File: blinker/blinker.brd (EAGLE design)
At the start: 36.5 x 64.8 mm, 11 parts, among them IC1 LM555D, SW1 SPST_TACT5.2VARIANT

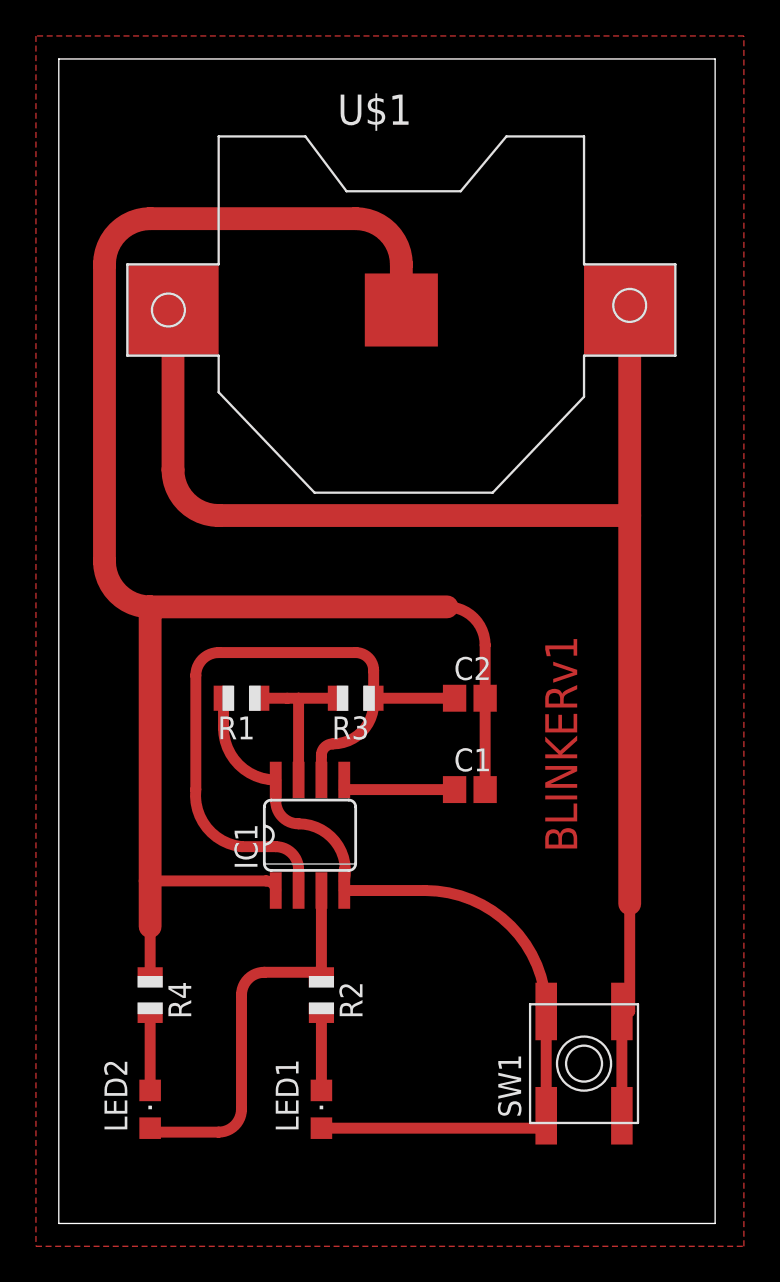
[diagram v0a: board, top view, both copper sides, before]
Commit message: CR2032 Batt holder amended, PCB design update
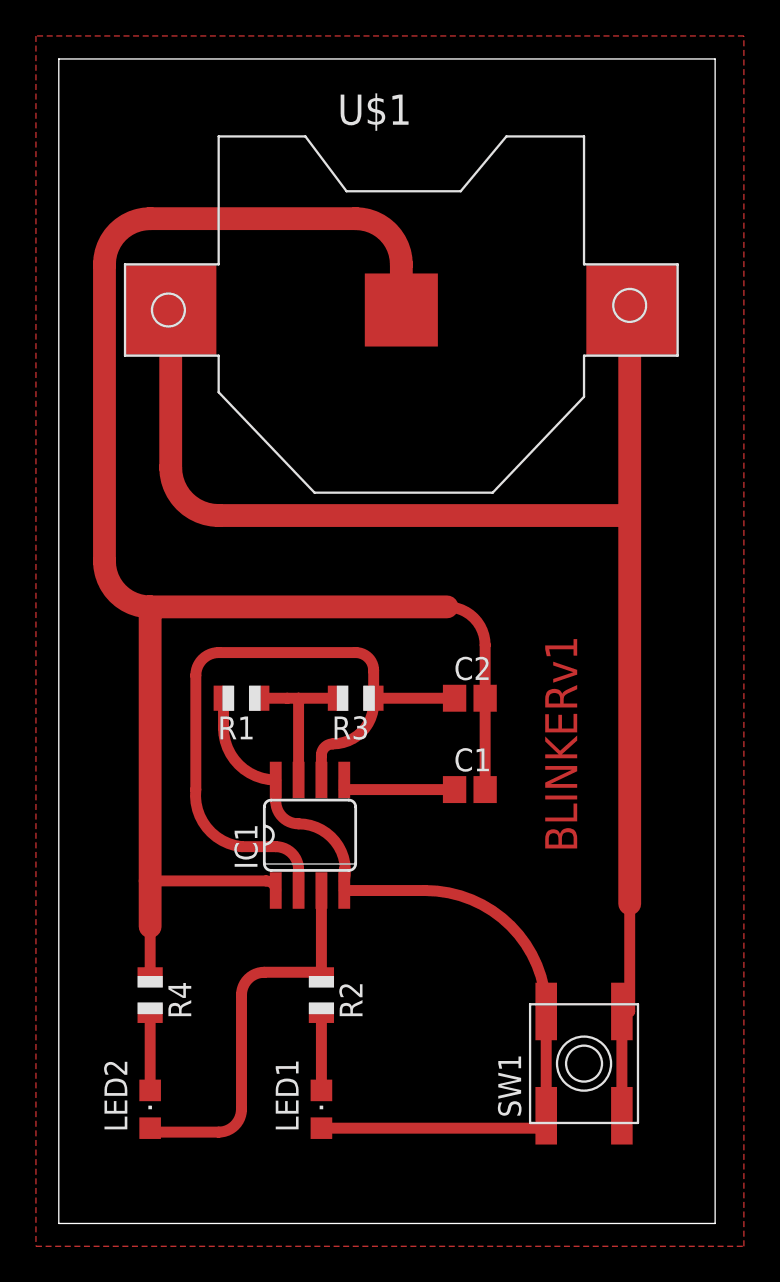
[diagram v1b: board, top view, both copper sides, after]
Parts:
- U$1: device adafruit:CR2032-SMD -> mokerek:CR2032-SMD
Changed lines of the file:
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@@
 <element name="R3" library="adafruit" package="R0805" value="100k" x="16.51" y="29.21" rot="R180"/>
 <element name="R4" library="adafruit" package="R0805" value="100" x="5.08" y="12.7" rot="R270"/>
-<element name="U$1" library="adafruit" package="CR2032-SMD" value="CR2032" x="19.05" y="50.8"/>
+<element name="U$1" library="mokerek" package="CR2032-SMD" value="CR2032" x="19.05" y="50.8"/>
 <element name="SW1" library="mokerek" package="5.2X5.2" value="SPST_TACT5.2VARIANT" x="29.21" y="8.89" rot="R90"/>
 </elements>
@@
 <contactref element="SW1" pad="A"/>
 <contactref element="U$1" pad="+$2"/>
-<wire x1="6.35" y1="50.8" x2="6.35" y2="41.91" width="1.27" layer="1"/>
-<wire x1="6.35" y1="41.91" x2="8.89" y2="39.37" width="1.27" layer="1" curve="90"/>
 <wire x1="8.89" y1="39.37" x2="31.75" y2="39.37" width="1.27" layer="1"/>
-<wire x1="31.75" y1="39.37" x2="31.75" y2="50.8" width="1.27" layer="1"/>
-<wire x1="31.75" y1="39.37" x2="31.75" y2="17.78" width="1.27" layer="1"/>
 <wire x1="31.314" y1="5.99" x2="31.314" y2="11.79" width="0.6096" layer="1"/>
 <wire x1="31.314" y1="11.79" x2="31.75" y2="11.79" width="0.6096" layer="1"/>
 <wire x1="31.75" y1="11.79" x2="31.75" y2="17.78" width="0.6096" layer="1"/>
+<wire x1="8.89" y1="39.37" x2="6.223" y2="42.037" width="1.27" layer="1" curve="-90"/>
+<wire x1="6.223" y1="42.037" x2="6.223" y2="50.8" width="1.27" layer="1"/>
+<wire x1="31.877" y1="50.8" x2="31.75" y2="50.673" width="1.27" layer="1" curve="90"/>
+<wire x1="31.75" y1="50.673" x2="31.75" y2="17.78" width="1.27" layer="1"/>
+<wire x1="31.75" y1="50.673" x2="31.75" y2="39.37" width="0" layer="19" extent="1-1"/>
 </signal>
 </signals>
+<errors>
+</errors>
 </board>
 </drawing>
